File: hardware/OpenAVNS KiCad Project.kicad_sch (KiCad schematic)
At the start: 166 parts, among them J1 Conn_ARM_JTAG_SWD_10, J2 USB_C_Receptacle, J3 Conn_01x02_Pin, Q1 BCV62, Q2 BC847, Q3 BC857, Q4 BCV61, Q5 BCV62, Q6 BC847, Q7 BC857, Q8 BCV61, SW1 SW_SPDT, T1 40uH 1:10 Wurth 750315839, U1 TS5A3159AYZPR, U10 OPA455, U11 LIS2DH12, U12 OPA455, U13 74AUC1G74, U14 TPS61200DRC, U15 OPA455, U16 LT1615ES5_TRPBF, U17 LT8304IS8E_PBF, U18 MCP73831-2-OT, U2 TLV9004xRUCR, U3 MCP4725xxx-xCH, U4 TS5A3159AYZPR, U5 nRF52840, U6 TS5A3159AYZPR, U7 MCP4725xxx-xCH, U8 TS5A3159AYZPR, U9 TLV9062, Y1 32MHz

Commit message: Updated footprints in schematic
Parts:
- removed T1: 40uH 1:10 Wurth 750315839, symbol Device:Transformer_1P_1S
- added C49: 100uF Electrolytic, 200V, Capacitor_THT:CP_Radial_D12.5mm_P5.00mm, symbol Device:C
- added T2: Wurth 750315839 - 1:10, 40uH, 750315839:WE-FLYLT_EP13_5465, symbol Wurth 750315839:750315839
- C1, C5, C6, C8: footprint (none) -> Capacitor_SMD:C_0603_1608Metric
- C10, C11, C14, C17, C3, C4, C7, R10, R22, R23, R24, R29, R3, R30, R31, R4, R5, R8, R9: footprint (none) -> Capacitor_SMD:C_0402_1005Metric
- C12, C15, C19: footprint Capacitor_SMD:C_0402_1005Metric -> Capacitor_SMD:C_1210_3225Metric
- C22, C43, C44, C48: footprint Capacitor_SMD:C_0402_1005Metric -> Capacitor_SMD:C_0603_1608Metric
- C23, C25, C37, C38: footprint Capacitor_SMD:C_0805_2012Metric -> Capacitor_SMD:C_0603_1608Metric
- C27, C29, C30, C31, C36: footprint Capacitor_SMD:C_0805_2012Metric -> Capacitor_SMD:C_1210_3225Metric
- C33: value 10uF, 50V -> 22uF, 50V
- C45, C46: value 10uF, 100V -> 22uF, 100V; footprint Capacitor_SMD:C_0805_2012Metric -> Capacitor_SMD:C_1210_3225Metric
- D12, D13: footprint LED_SMD:LED_0805_2012Metric_Pad1.15x1.40mm_HandSolder -> LED_SMD:LED_0402_1005Metric
- L1: value 4.7nH -> 4.7nH, 5%; footprint (none) -> Inductor_SMD:L_0402_1005Metric
- L3: footprint Inductor_SMD:L_1008_2520Metric_Pad1.43x2.20mm_HandSolder -> Inductor_SMD:L_7.3x7.3_H3.5
- R1, R15, R16, R19, R2, R20, R27, R28, R32, R33, R6, R7: footprint (none) -> Capacitor_SMD:C_0805_2012Metric
- R11, R14, R17, R18, R49, R53, R54, R56, R57, R62: footprint Resistor_SMD:R_0805_2012Metric_Pad1.20x1.40mm_HandSolder -> Resistor_SMD:R_0603_1608Metric_Pad0.98x0.95mm_HandSolder
- R12, R13, R21, R25, R26, R34, R35, R36, R37, R39, R41, R42, R43, R45, R47, R48, R50, R51, R60, R61, R65, R66, R67, R68: footprint Resistor_SMD:R_0805_2012Metric_Pad1.20x1.40mm_HandSolder -> Resistor_SMD:R_0402_1005Metric
- R38, R40, R44, R46: footprint Resistor_SMD:R_0805_2012Metric_Pad1.20x1.40mm_HandSolder -> Resistor_SMD:R_1206_3216Metric
- R59, R64: footprint Resistor_SMD:R_0805_2012Metric_Pad1.20x1.40mm_HandSolder -> Resistor_SMD:R_0603_1608Metric
- U10, U12, U15: footprint (none) -> Package_SO:TI_SO-PowerPAD-8_ThermalVias
- U9: footprint (none) -> OpenAVNS:QFN50P200X150X40-10N
- Y1: footprint (none) -> Crystal:Crystal_SMD_2016-4Pin_2.0x1.6mm
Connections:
- net +50V: now also C49.1
- net -50V: now also C49.2, T2.9
- net V_ON: now also T2.3
- net at R58.2, U17.5 (SW): now also T2.5
- net at D9.2 (A): now also T2.7
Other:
- moved on the sheet: C29, C30, C31, C38, D9, R52, R55, U15

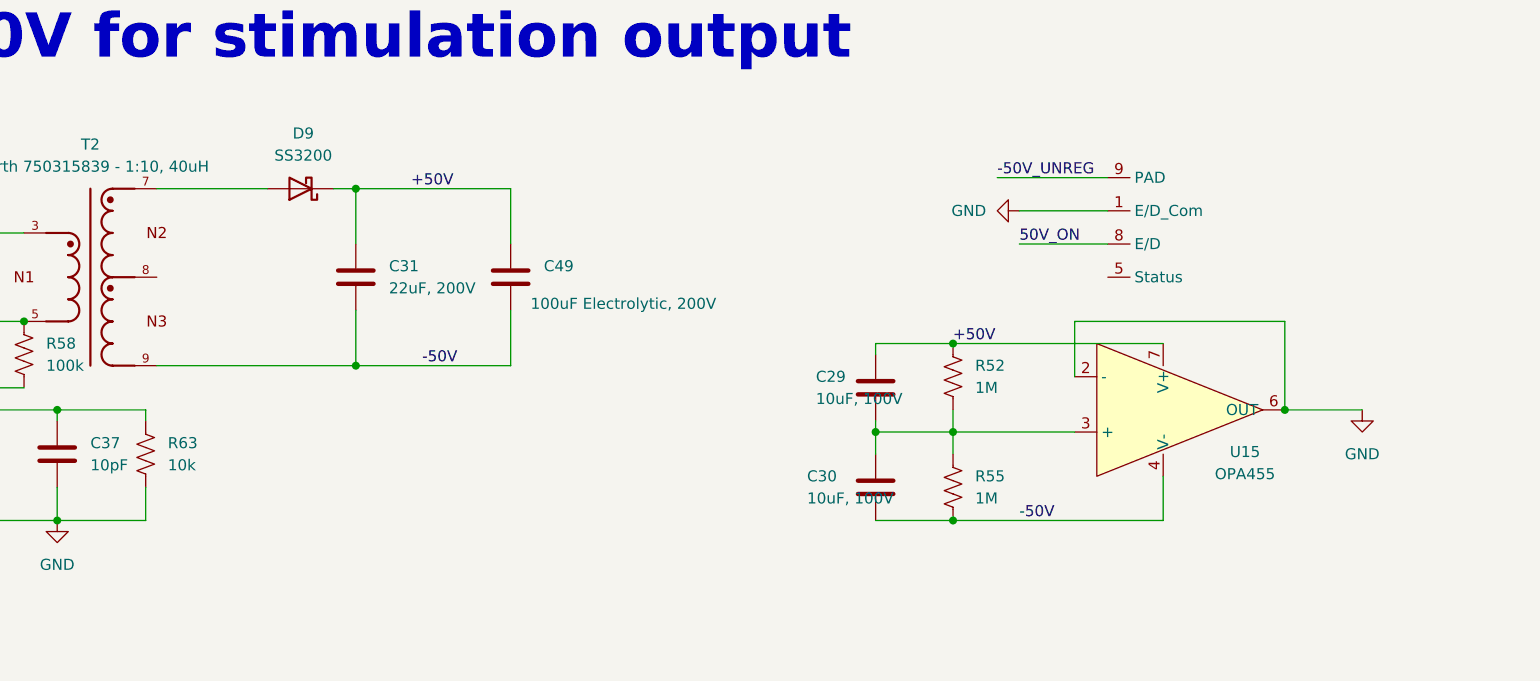
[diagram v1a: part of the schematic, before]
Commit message: Changed 50V converter config, eliminating op amp. Also changed some footprints (work in progress)
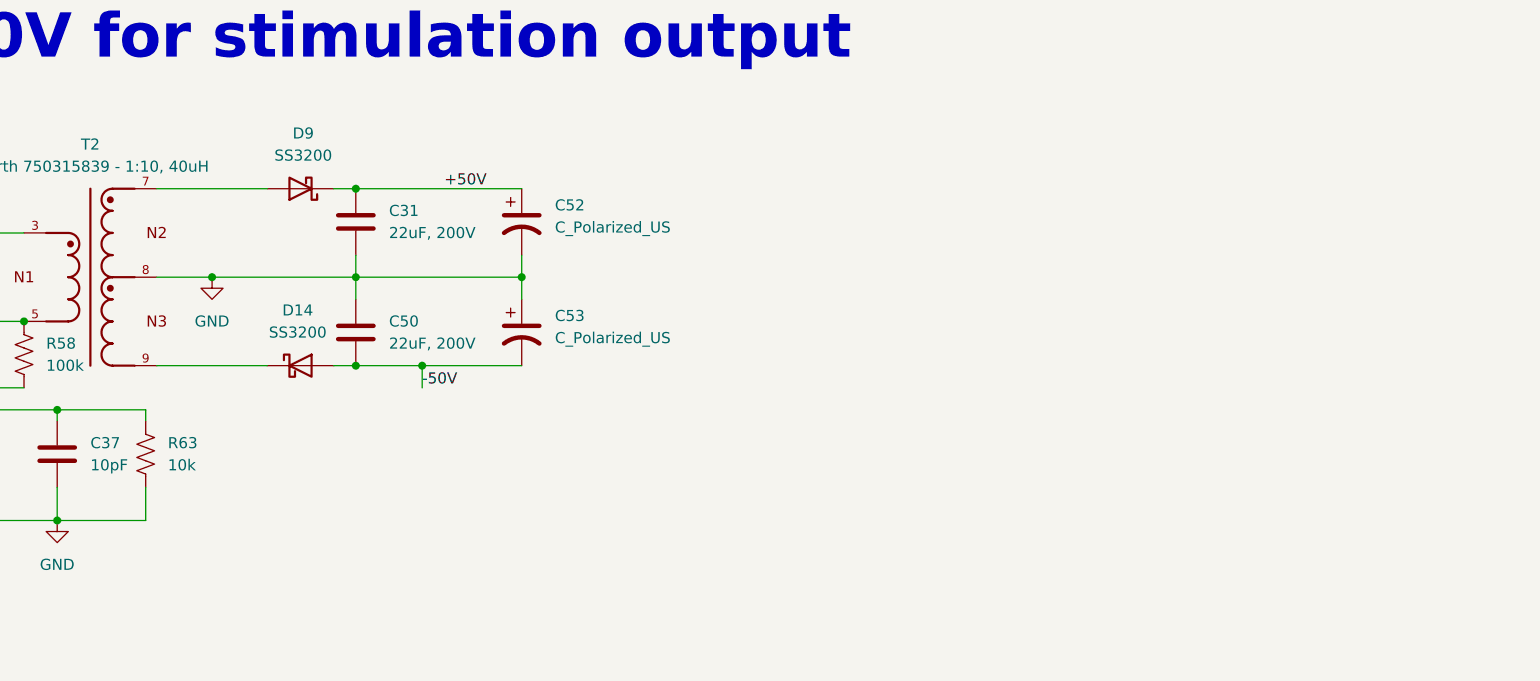
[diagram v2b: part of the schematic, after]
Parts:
- removed C29, C30: 10uF, 100V, Capacitor_SMD:C_1210_3225Metric, symbol Device:C
- removed C49: 100uF Electrolytic, 200V, Capacitor_THT:CP_Radial_D12.5mm_P5.00mm, symbol Device:C
- removed R52, R55: 1M, Resistor_SMD:R_0805_2012Metric_Pad1.20x1.40mm_HandSolder, symbol Device:R_US
- removed U15: OPA455, Package_SO:TI_SO-PowerPAD-8_ThermalVias, symbol Amplifier_Operational:OPA455
- added C50: 22uF, 200V, Capacitor_SMD:C_1210_3225Metric, symbol Device:C
- added C52, C53: C_Polarized_US, Capacitor_THT:CP_Radial_D12.5mm_P5.00mm, symbol Device:C_Polarized_US
- added D14: SS3200, Diode_SMD:D_SMA, symbol Diode:SS3200
- S1: footprint 5-1437565-0:SW_5-1437565-0 -> Button_Switch_SMD:SW_SPST_PTS647_Sx38
- SW1: footprint Button_Switch_SMD:SW_SPDT_CK-JS102011SAQN -> Button_Switch_SMD:SW_SPDT_CK_JS102011SAQN
- T2: footprint 750315839:WE-FLYLT_EP13_5465 -> OpenAVNS:WE-FLYLT_EP13_5465
- U16: footprint LT1615ES5_TRPBF:SOT95P280X145-5N -> OpenAVNS:SOT95P280X145-5N
- U17: footprint LT8304IS8E_PBF:SOIC127P599X175-9N -> OpenAVNS:SOIC127P599X175-9N
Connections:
- net +50V: now also C52.1
- net -50V: now also C50.2, C53.2, D14.2 (A); no longer C31.2, T2.9
- net GND: now also C31.2, T2.8, C50.1, C52.2, C53.1
- new net: D14.1 (K), T2.9
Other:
- moved on the sheet: C31

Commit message: Fixed some schematic parts, added test points and 3.5mm jack for output
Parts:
- removed Y1: 32MHz, Crystal:Crystal_SMD_2016-4Pin_2.0x1.6mm, symbol Device:Crystal
- added J2: AudioPlug3, Connector_Audio:Jack_3.5mm_CUI_SJ-3523-SMT_Horizontal, symbol Connector_Audio:AudioPlug3
- added TP1, TP10, TP11, TP12, TP13, TP14, TP15, TP16, TP17, TP18, TP19, TP2, TP20, TP21, TP22, TP23, TP24, TP25, TP26, TP27, TP28, TP29, TP3, TP30, TP31, TP32, TP33, TP34, TP35, TP36, TP37, TP38, TP39, TP4, TP40, TP5, TP6, TP7, TP8, TP9: TestPoint, TestPoint:TestPoint_Pad_D2.0mm, symbol Connector:TestPoint
- added Y1: 32MHz - X322532MOB4SI, Crystal:Crystal_SMD_3225-4Pin_3.2x2.5mm, symbol Device:Crystal_GND24
- AT1: footprint 2450AT43B100E:ANTENNA_2450AT43B100E -> OpenAVNS:ANTENNA_2450AT43B100E
- renumbered C45 to C15, C46 to C16, C15 to C17, C44 to C18, C41 to C19, C16 to C20, C17 to C21, C18 to C22, C19 to C23, C20 to C24, C21 to C25, C22 to C26, C47 to C27, C48 to C28, C43 to C29, C42 to C30, C23 to C31, C24 to C32, C25 to C33, C26 to C34, C27 to C35, C28 to C36, C31 to C37, C52 to C38, C32 to C39, C50 to C40, C53 to C41, C33 to C42, C34 to C43, C35 to C44, C36 to C45, C38 to C46, C37 to C47, C39 to C48, C40 to C49, D14 to D11, D11 to D12, D12 to D13, D13 to D14, J2 to J3, J3 to J4, R53 to R52, R54 to R53, R56 to R54, R57 to R55, R58 to R56, R59 to R57, R60 to R58, R61 to R59, R62 to R60, R63 to R61, R64 to R62, R65 to R63, R66 to R64, R67 to R65, R68 to R66, T2 to T1, U9 to U10, U16 to U15, U17 to U16, U18 to U17, U10 to U9
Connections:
- net +20V: now also TP34.1
- net +3.3V: now also U10.7 (V+), TP28.1; no longer U10.8 (V+)
- net +50V: now also TP31.1
- net -20V: now also TP30.1
- net -50V: now also TP36.1
- net C1_Anodic: now also TP1.1
- net C1_Cathodic: now also TP6.1
- net C2_Anodic: now also TP10.1
- net C2_Cathodic: now also TP19.1
- net E1: now also J2.T, TP5.1
- net E2: now also J2.R, TP7.1
- net EmStop: now also TP25.1
- net GND: now also U10.1 (V-), U10.10 (+), U10.4 (+), TP17.1, TP8.1, Y1.2, Y1.4; no longer U10.3 (+), U10.4 (V-), U10.5 (+)
- net Ground_Electrode: now also J2.S, TP9.1
- net HV_CLK: now also TP27.1
- net HV_EN: now also TP23.1
- net HV_ON: now also TP24.1, TP32.1
- net SWO: now also TP14.1
- net VBAT: now also TP37.1, TP40.1
- net V_ON: now also TP38.1
- net V_USB: now also TP39.1
- net Z1: now also U10.8, TP21.1; no longer U10.1
- net Z2: now also U10.6, TP26.1; no longer U10.7
- net Z_ON: now also U10.2 (nSHDN1), U10.3 (nSHDN2)
- net at D4.2 (A), R38.1: now also TP20.1
- net at R34.2, R35.1, R39.1: now also U10.9 (-); no longer U10.2 (-)
- net at R56.2, T1.5, U16.5 (SW): now also TP35.1
- net at U1.C2, U3.1 (VOUT), U4.C2: now also TP3.1
- net at R41.2, R42.1, R45.1: now also U10.5 (-); no longer U10.6 (-)
- net at Q7.2 (E), R28.1, R29.2: now also TP18.1
- net at Q2.2 (E), R5.2, R6.2: now also TP2.1
- net at C36.2, C39.1, L3.2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: now also TP33.1
- net at C21.1, U5.A23 (XC2): now also Y1.1
- net at J1.4 (SWCLK/TCK), U5.AA24 (SWDCLK): now also TP12.1
- net at J1.10 (~{RESET}), U5.AC13 (P0.18/~{RESET}): now also TP11.1
- net at J1.2 (SWDIO/TMS), U5.AC24 (SWDIO): now also TP13.1
- net at C14.2, U5.B24 (XC1): now also Y1.3
- net at Q6.2 (E), R24.2, R27.2: now also TP15.1
- net at D6.2 (A), R44.1: now also TP22.1
- net at Q3.2 (E), R7.1, R8.2: now also TP4.1
- net at R48.2, R51.1, U14.10 (FB): now also TP29.1
- net at U6.C2, U7.1 (VOUT), U8.C2: now also TP16.1
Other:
- moved on the sheet: C29, C30

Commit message: Updated 50V cap values and size
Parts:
- C38, C41: value C_Polarized_US -> 10uF, 100V electrolytic; footprint Capacitor_THT:CP_Radial_D12.5mm_P5.00mm -> Capacitor_THT:CP_Radial_D6.3mm_P2.50mm
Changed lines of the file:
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@@
 			)
 		)
-		(property "Value" "C_Polarized_US"
+		(property "Value" "10uF, 100V electrolytic"
 			(at 601.98 495.9349 0)
 			(effects
@@
 			)
 		)
-		(property "Footprint" "Capacitor_THT:CP_Radial_D12.5mm_P5.00mm"
+		(property "Footprint" "Capacitor_THT:CP_Radial_D6.3mm_P2.50mm"
 			(at 598.17 495.3 0)
 			(effects
@@
 			)
 		)
-		(property "Description" "Polarized capacitor, US symbol"
+		(property "Description" "Polarized capacitor, US symbol - JLCPCB #C2029"
 			(at 598.17 495.3 0)
 			(effects
@@
 			)
 		)
-		(property "Value" "C_Polarized_US"
+		(property "Value" "10uF, 100V electrolytic"
 			(at 601.98 508.6349 0)
 			(effects
@@
 			)
 		)
-		(property "Footprint" "Capacitor_THT:CP_Radial_D12.5mm_P5.00mm"
+		(property "Footprint" "Capacitor_THT:CP_Radial_D6.3mm_P2.50mm"
 			(at 598.17 508 0)
 			(effects
@@
 			)
 		)
-		(property "Description" "Polarized capacitor, US symbol"
+		(property "Description" "Polarized capacitor, US symbol - JLCPCB #C2029"
 			(at 598.17 508 0)
 			(effects

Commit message: Some lazy Saturday floorplanning on the layout
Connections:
- net E1_Pre: no longer U12.3 (+)
- net E2_Pre: now also U12.3 (+)
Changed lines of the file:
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@@
 		)
 	)
-	(label "E1_Pre"
+	(label "E2_Pre"
 		(at 435.61 370.84 0)
 		(effects

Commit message: Started doing proper layout
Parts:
- removed TP40: TestPoint, TestPoint:TestPoint_Pad_D2.0mm, symbol Connector:TestPoint
- added L4: 2.7nH, 5%, Inductor_SMD:L_0402_1005Metric, symbol Device:L
- added L5: 1.8nH, 5%, Inductor_SMD:L_0402_1005Metric, symbol Device:L
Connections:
- net GND: now also L5.1
- net RF_ANT: now also L4.2, L5.2; no longer AT1.1
- new net: AT1.1, L4.1
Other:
- moved on the sheet: AT1

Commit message: First draft of layout, still has work to be done
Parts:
- added J5: Conn_01x03_Pin, Connector_PinHeader_2.54mm:PinHeader_1x03_P2.54mm_Vertical, symbol Connector:Conn_01x03_Pin
- added R67, R68: 100k, Resistor_SMD:R_0402_1005Metric, symbol Device:R_US
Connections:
- net E1: now also J5.1 (Pin_1)
- net E2: now also J5.2 (Pin_2)
- net GND: now also R68.1
- net Ground_Electrode: now also J5.3 (Pin_3)
- net VBAT: now also R67.2
- net Batt_Measure: now reaches U5.H2 (P0.27)
- net Batt_Measure: now also R67.1, R68.2

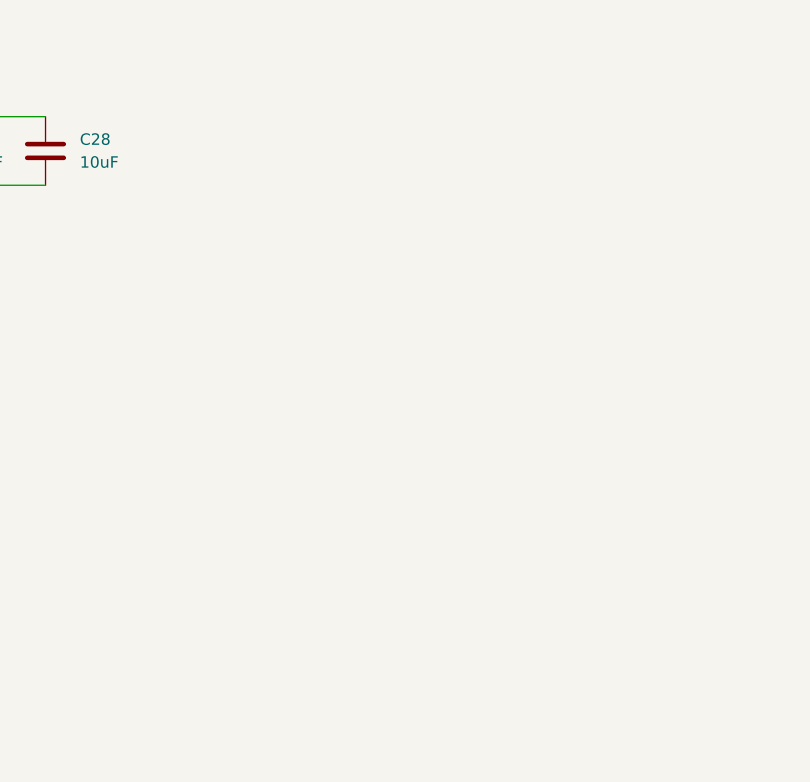
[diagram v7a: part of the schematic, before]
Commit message: Added mounting holes
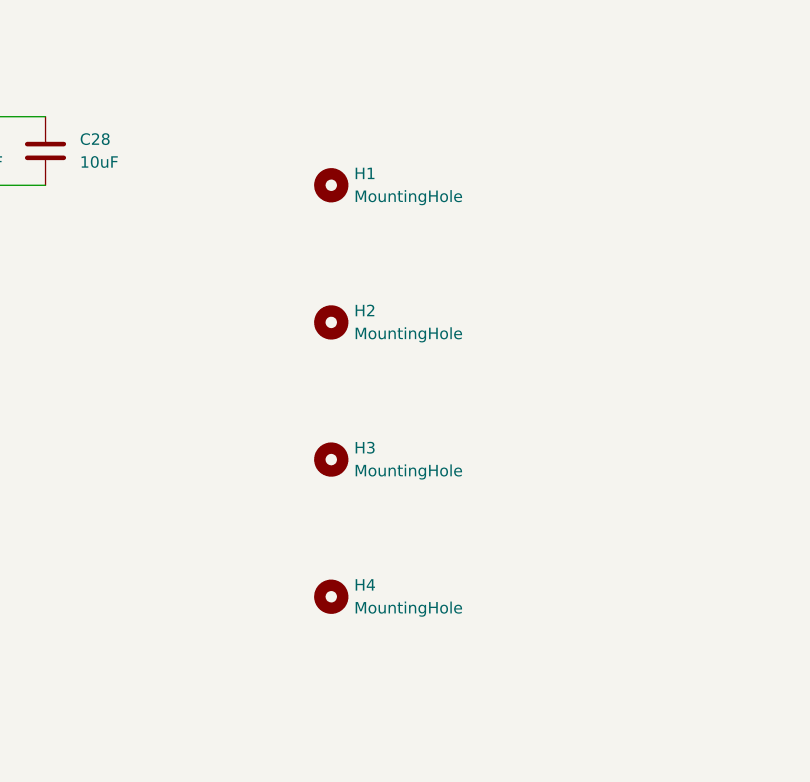
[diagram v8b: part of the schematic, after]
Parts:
- added H1, H2, H3, H4: MountingHole, MountingHole:MountingHole_3.2mm_M3_DIN965, symbol Mechanical:MountingHole
